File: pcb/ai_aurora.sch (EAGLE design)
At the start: 1 part

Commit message: schematic done
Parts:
- added BAT1, BAT2: (no value), Ai_Electromechanical:BATTERY-HOLDER
- added C1, C2, C3: (no value), Ai_Passives:CAP025X050
- added D1: (no value), Ai_DiscreteSemis:DIODETH-1N914
- added IC1: ATTINY85-DIP, Ai_IC:ATTINY85-DIP
- added J1: 1X02ST, Ai_Connectors:1X02ST
- added J2: 2X03, Ai_Connectors:2X03
- added LDR: LDR-PTH, Ai_Sensors:LDR-PTH
- added Q3: (no value), Ai_DiscreteSemis:TRANSISTOR-NPN
- added Q4: (no value), Ai_DiscreteSemis:TRANSISTOR-PNP
- added R2: 1K, Ai_Passives:RESAXIAL-0.4
- added R5: 100K, Ai_Passives:RESAXIAL-0.4
- added R6: 10K, Ai_Passives:RESAXIAL-0.4
- added R7: 1M, Ai_Passives:RESAXIAL-0.4
- added U$4, U$5: LED-PL9823-F8, Ai_LED:LED-PL9823-F8
- R1: value LDR-PTH -> 1K; device Ai_Sensors:LDR-PTH -> Ai_Passives:RESAXIAL-0.4
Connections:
- new net +: C1.1, C2.1, IC1.VCC, J2.2, Q4.C, R2.2
- new net -: C1.2, C2.2, IC1.GND, J2.6, R1.2, R7.1
- new net DI: IC1.PB3/ADC3, U$4.DI
- new net DO: U$5.DO
- new net GND: C3.2, J1.2, LDR.P$1, Q3.E, R1.1
- new net MISO: IC1.PB1/MISO, J2.1
- new net MOSI: IC1.PB0/MOSI, J2.4
- new net N$1: BAT1.+, BAT2.-
- new net N$10: LDR.P$2, Q3.B, R5.1, R7.2
- new net N$12: Q3.C, R6.2
- new net N$13: Q4.B, R6.1
- new net N$2: D1.A, J1.1
- new net N$4: U$4.DO, U$5.DI
- new net N$6: U$4.VDD, U$5.VDD
- new net N$7: U$4.VSS, U$5.VSS
- new net RST: IC1.PB5/!RES, J2.5, R2.1
- new net SCK: IC1.PB2/SCK/ADC1, J2.3
- new net VBAT: BAT2.+, Q4.E, R5.2
- new net VIN: BAT1.-, C3.1, D1.C

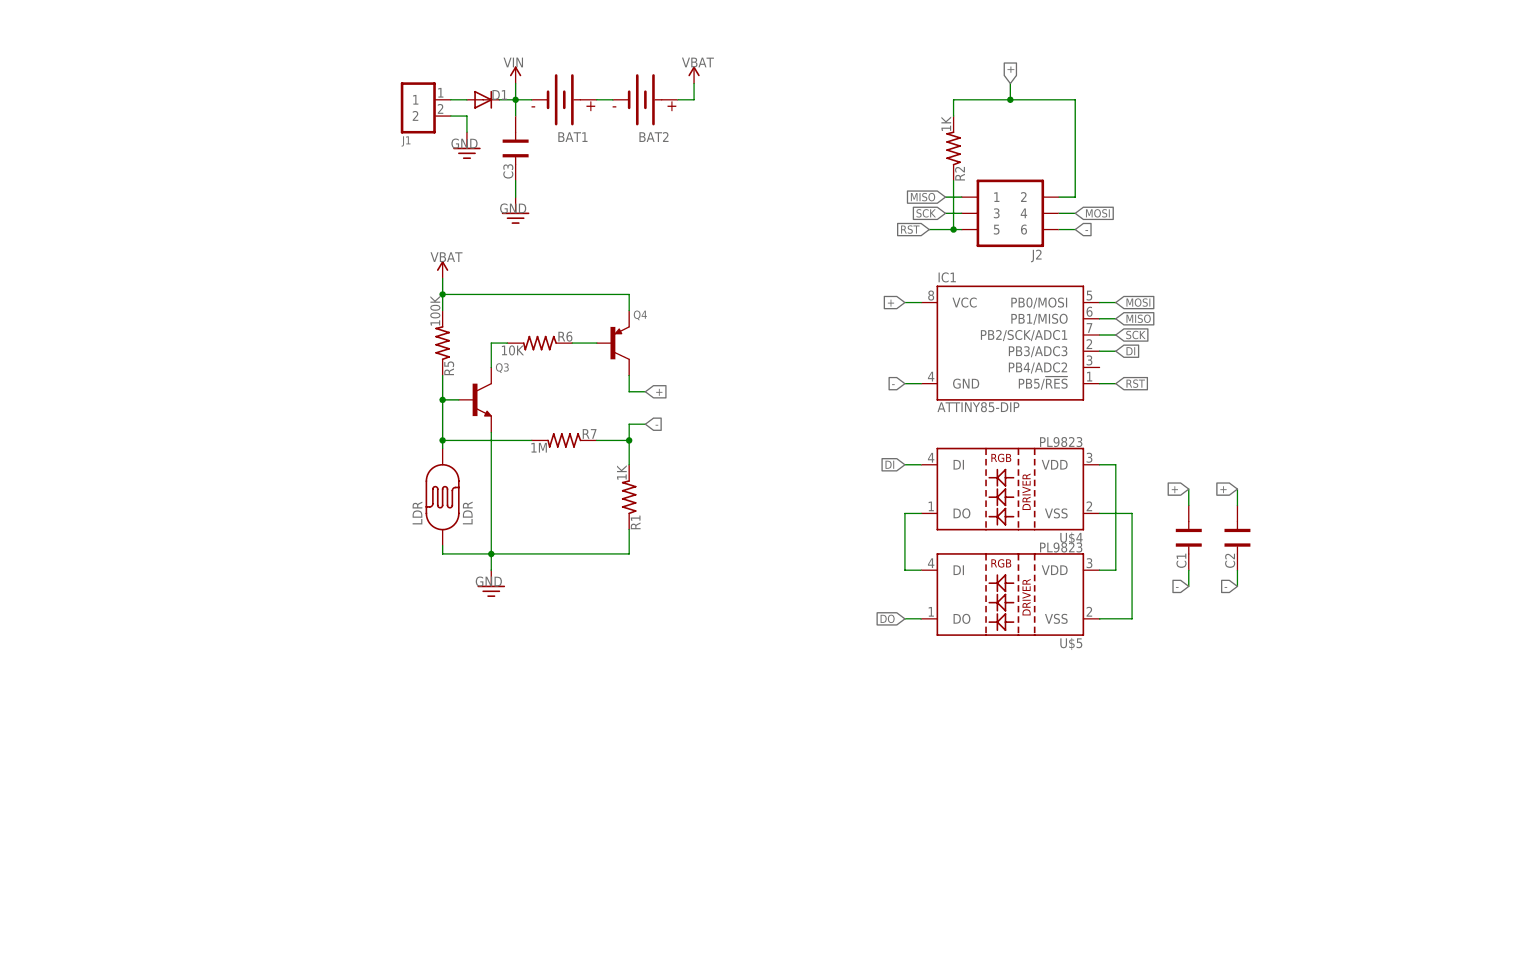
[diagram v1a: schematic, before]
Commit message: some fitting issues remain
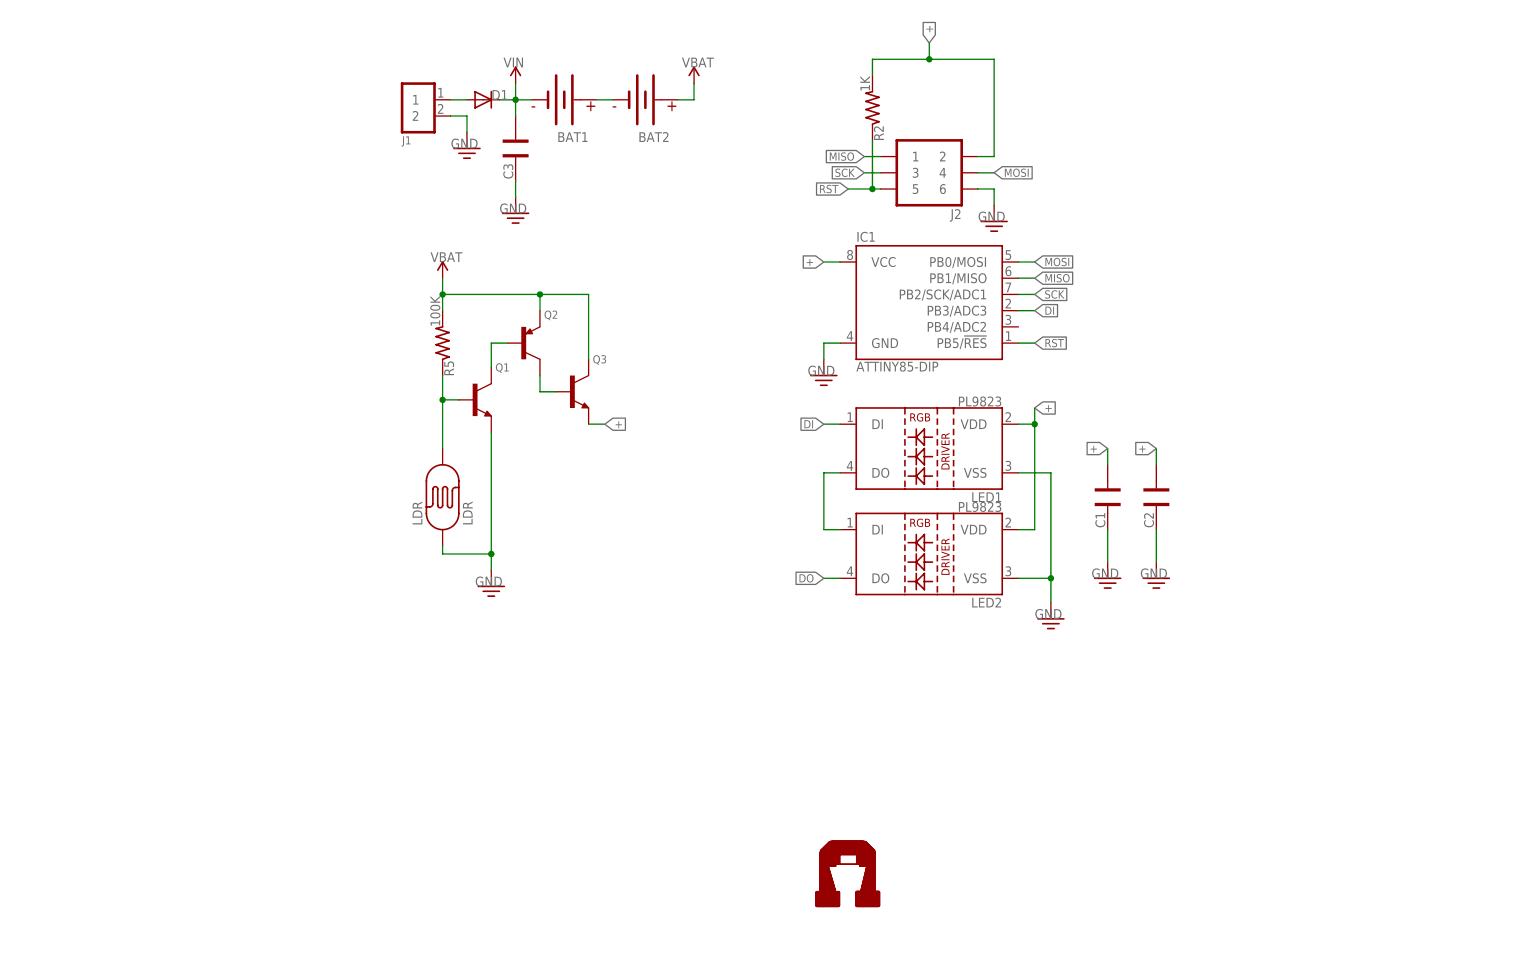
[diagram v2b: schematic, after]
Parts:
- removed Q4: (no value), Ai_DiscreteSemis:TRANSISTOR-PNP
- removed R1: 1K, Ai_Passives:RESAXIAL-0.4
- removed R6: 10K, Ai_Passives:RESAXIAL-0.4
- removed R7: 1M, Ai_Passives:RESAXIAL-0.4
- added LED1, LED2: LED-PL9823-F8, Ai_LED:LED-PL9823-F8
- added Q1: (no value), Ai_DiscreteSemis:TRANSISTOR-NPN
- added Q2: (no value), Ai_DiscreteSemis:TRANSISTOR-PNP
- BAT1, BAT2: device Ai_Electromechanical:BATTERY-HOLDER -> Ai_Electromechanical:BATTERY-HOLDERCR123A
- U$4, U$5: value LED-PL9823-F8 -> AI-LOGOM; device Ai_LED:LED-PL9823-F8 -> Ai_Miscellany:AI-LOGOM
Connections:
- removed net -: C1.2, C2.2, IC1.GND, J2.6, R1.2, R7.1
- removed net N$12: Q3.C, R6.2
- removed net N$6: U$4.VDD, U$5.VDD
- removed net N$7: U$4.VSS, U$5.VSS
- net +: now also LED1.VDD, LED2.VDD, Q2.C, Q3.B, Q3.E; no longer Q4.C
- net DI: now also LED1.DI; no longer U$4.DI
- net DO: now also LED2.DO; no longer U$5.DO
- net GND: now also C1.2, C2.2, IC1.GND, J2.6, LED1.VSS, LED2.VSS, Q1.E; no longer Q3.E, R1.1
- net N$10: now also Q1.B; no longer Q3.B, R7.2
- net N$13: now also Q1.C, Q2.B; no longer Q4.B, R6.1
- net N$4: now also LED1.DO, LED2.DI; no longer U$4.DO, U$5.DI
- net VBAT: now also Q2.E, Q3.C; no longer Q4.E
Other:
- moved on the sheet: C1, C2, IC1, J2, Q3, R2

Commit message: updating firmware and pcb
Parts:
- removed LDR: LDR-PTH, Ai_Sensors:LDR-PTH
- removed Q2: (no value), Ai_DiscreteSemis:TRANSISTOR-PNP
- removed Q3: (no value), Ai_DiscreteSemis:TRANSISTOR-NPN
- added JP1, JP2: 1X02-PJ, Ai_Connectors:1X02-PJ
- added LDR1: LDR-PTH, Ai_Sensors:LDR-PTH
- added R1: 10K, Ai_Passives:RESAXIAL-0.4
- added S1, S2: SW-SPSTTH06X06, Ai_Electromechanical:SW-SPSTTH06X06
- added VR1: 1M, Ai_Passives:POT05X05
- C3: value (none) -> 4.7uF; device Ai_Passives:CAP025X050 -> Ai_Passives:CAP-POL025X50
- Q1: value (none) -> FQP30N06L; device Ai_DiscreteSemis:TRANSISTOR-NPN -> Ai_DiscreteSemis:FET-NMOS-FQP30N06L
- R2: value 1K -> 10K
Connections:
- net MOSI renamed MOSI/SET
- removed net MISO: IC1.PB1/MISO, J2.1
- removed net N$10: LDR.P$2, Q1.B, R5.1
- removed net N$13: Q1.C, Q2.B
- removed net SCK: IC1.PB2/SCK/ADC1, J2.3
- new net -: C1.2, C2.2, LED1.VSS, LED2.VSS, Q1.D
- new net LED_EN: IC1.PB4/ADC2, Q1.G
- new net MISO/LDR: IC1.PB1/MISO, J2.1, JP1.1
- new net N$3: R1.2, S1.B@1
- new net N$5: R2.2, S2.A@1
- new net N$6: R5.2, VR1.S
- new net N$7: JP1.2, LDR1.P$2, R5.1
- new net SCK/BATT: IC1.PB2/SCK/ADC1, J2.3, JP2.1
- net +: no longer IC1.VCC, J2.2, Q2.C, Q3.B, Q3.E, R2.2
- net GND: now also C3.C, LDR1.P$1, Q1.S, R1.1, R2.1; no longer C1.2, C2.2, C3.2, LDR.P$1, LED1.VSS, LED2.VSS, Q1.E
- net RST: now also S1.A@1; no longer R2.1
- net VBAT: now also IC1.VCC, J2.2, JP2.2, VR1.A; no longer Q2.E, Q3.C, R5.2
- net VIN: now also C3.A; no longer C3.1
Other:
- moved on the sheet: BAT1, BAT2, C1, C2, D1, IC1, J1, J2, LED1, LED2, R2, R5

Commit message: updating
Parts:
- removed R5: 100K, Ai_Passives:RESAXIAL-0.4
- added R3: 10K, Ai_Passives:RESAXIAL-0.4
- added R4: 100K, Ai_Passives:RESAXIAL-0.4
- R2: value 10K -> 100K
- renumbered C3 to C11
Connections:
- net GND: now also R3.1, R4.1; no longer R2.1
- net LED_EN: now also R4.2
- net N$5: now also R3.2; no longer R2.2
- net N$6: now also R2.2; no longer R5.2
- net N$7: now also R2.1; no longer R5.1
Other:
- moved on the sheet: R2
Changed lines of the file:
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@@
 <part name="IC1" library="Ai_IC" deviceset="ATTINY" device="85-DIP"/>
 <part name="LDR1" library="Ai_Sensors" deviceset="LDR" device="-PTH"/>
-<part name="R5" library="Ai_Passives" deviceset="RES" device="AXIAL-0.4" value="100K"/>
+<part name="R2" library="Ai_Passives" deviceset="RES" device="AXIAL-0.4" value="100K"/>
 <part name="GND5" library="Ai_Power" deviceset="GND" device=""/>
 <part name="U$2" library="Ai_Power" deviceset="VBAT" device=""/>
@@
 <part name="GND1" library="Ai_Power" deviceset="GND" device=""/>
 <part name="U$3" library="Ai_Power" deviceset="VBAT" device=""/>
-<part name="C3" library="Ai_Passives" deviceset="CAP-POL" device="025X50" value="4.7uF"/>
+<part name="C11" library="Ai_Passives" deviceset="CAP-POL" device="025X50" value="4.7uF"/>
 <part name="GND2" library="Ai_Power" deviceset="GND" device=""/>
 <part name="GND3" library="Ai_Power" deviceset="GND" device=""/>
@@
 <part name="GND6" library="Ai_Power" deviceset="GND" device=""/>
 <part name="S2" library="Ai_Electromechanical" deviceset="SW-SPST" device="TH06X06"/>
-<part name="R2" library="Ai_Passives" deviceset="RES" device="AXIAL-0.4" value="10K"/>
+<part name="R3" library="Ai_Passives" deviceset="RES" device="AXIAL-0.4" value="10K"/>
 <part name="GND7" library="Ai_Power" deviceset="GND" device=""/>
+<part name="R4" library="Ai_Passives" deviceset="RES" device="AXIAL-0.4" value="100K"/>
 </parts>
 <sheets>
@@
 <instance part="IC1" gate="G$1" x="137.16" y="101.6"/>
 <instance part="LDR1" gate="G$1" x="82.55" y="97.79" rot="R90"/>
-<instance part="R5" gate="G$1" x="82.55" y="113.03" rot="MR90"/>
+<instance part="R2" gate="G$1" x="82.55" y="113.03" rot="MR90"/>
 <instance part="GND5" gate="GND" x="82.55" y="86.36"/>
 <instance part="U$2" gate="G$1" x="82.55" y="128.27"/>
@@
 <instance part="GND1" gate="GND" x="27.94" y="107.95"/>
 <instance part="U$3" gate="G$1" x="63.5" y="118.11"/>
-<instance part="C3" gate="G$1" x="35.56" y="107.95"/>
+<instance part="C11" gate="G$1" x="35.56" y="107.95"/>
 <instance part="GND2" gate="GND" x="35.56" y="97.79"/>
 <instance part="GND3" gate="GND" x="119.38" y="90.17"/>
@@
 <instance part="Q1" gate="G$1" x="191.77" y="74.93"/>
 <instance part="U$8" gate="G$1" x="191.77" y="87.63"/>
-<instance part="GND6" gate="GND" x="191.77" y="64.77"/>
+<instance part="GND6" gate="GND" x="191.77" y="58.42"/>
 <instance part="S2" gate="G$1" x="92.71" y="74.93"/>
-<instance part="R2" gate="G$1" x="85.09" y="67.31" rot="R90"/>
+<instance part="R3" gate="G$1" x="85.09" y="67.31" rot="R90"/>
 <instance part="GND7" gate="GND" x="85.09" y="58.42"/>
+<instance part="R4" gate="G$1" x="182.88" y="68.58" rot="R90"/>
 </instances>
 <busses>
@@
 </segment>
 <segment>
-<pinref part="C3" gate="G$1" pin="C"/>
+<pinref part="C11" gate="G$1" pin="C"/>
 <pinref part="GND2" gate="GND" pin="GND"/>
 <wire x1="35.56" y1="100.33" x2="35.56" y2="102.87" width="0.1524" layer="91"/>
@@
 <segment>
 <pinref part="Q1" gate="G$1" pin="S"/>
-<wire x1="191.77" y1="69.85" x2="191.77" y2="67.31" width="0.1524" layer="91"/>
+<wire x1="191.77" y1="69.85" x2="191.77" y2="62.23" width="0.1524" layer="91"/>
 <pinref part="GND6" gate="GND" pin="GND"/>
-</segment>
-<segment>
-<pinref part="R2" gate="G$1" pin="1"/>
+<pinref part="R4" gate="G$1" pin="1"/>
+<wire x1="191.77" y1="62.23" x2="191.77" y2="60.96" width="0.1524" layer="91"/>
+<wire x1="191.77" y1="62.23" x2="182.88" y2="62.23" width="0.1524" layer="91"/>
+<wire x1="182.88" y1="62.23" x2="182.88" y2="63.5" width="0.1524" layer="91"/>
+<junction x="191.77" y="62.23"/>
+</segment>
+<segment>
+<pinref part="R3" gate="G$1" pin="1"/>
 <pinref part="GND7" gate="GND" pin="GND"/>
 <wire x1="85.09" y1="60.96" x2="85.09" y2="62.23" width="0.1524" layer="91"/>
@@
 <wire x1="35.56" y1="115.57" x2="38.1" y2="115.57" width="0.1524" layer="91"/>
 <junction x="35.56" y="115.57"/>
-<pinref part="C3" gate="G$1" pin="A"/>
+<pinref part="C11" gate="G$1" pin="A"/>
 <wire x1="35.56" y1="113.03" x2="35.56" y2="115.57" width="0.1524" layer="91"/>
 </segment>
@@
 <pinref part="Q1" gate="G$1" pin="G"/>
 <wire x1="185.42" y1="74.93" x2="182.88" y2="74.93" width="0.1524" layer="91"/>
-<label x="182.88" y="74.93" size="1.27" layer="95" font="vector" ratio="10" rot="R180" xref="yes"/>
+<label x="180.34" y="74.93" size="1.27" layer="95" font="vector" ratio="10" rot="R180" xref="yes"/>
+<pinref part="R4" gate="G$1" pin="2"/>
+<wire x1="182.88" y1="74.93" x2="180.34" y2="74.93" width="0.1524" layer="91"/>
+<wire x1="182.88" y1="73.66" x2="182.88" y2="74.93" width="0.1524" layer="91"/>
+<junction x="182.88" y="74.93"/>
 </segment>
 </net>
 <net name="N$6" class="0">
 <segment>
-<pinref part="R5" gate="G$1" pin="2"/>
+<pinref part="R2" gate="G$1" pin="2"/>
 <pinref part="VR1" gate="G$1" pin="S"/>
 <wire x1="82.55" y1="118.11" x2="82.55" y2="120.65" width="0.1524" layer="91"/>
@@
 <segment>
 <pinref part="LDR1" gate="G$1" pin="P$2"/>
-<pinref part="R5" gate="G$1" pin="1"/>
+<pinref part="R2" gate="G$1" pin="1"/>
 <wire x1="82.55" y1="105.41" x2="82.55" y2="106.68" width="0.1524" layer="91"/>
 <pinref part="JP1" gate="G$1" pin="2"/>
@@
 <net name="N$5" class="0">
 <segment>
-<pinref part="R2" gate="G$1" pin="2"/>
+<pinref part="R3" gate="G$1" pin="2"/>
 <wire x1="85.09" y1="72.39" x2="85.09" y2="74.93" width="0.1524" layer="91"/>
 <pinref part="S2" gate="G$1" pin="A@1"/>
